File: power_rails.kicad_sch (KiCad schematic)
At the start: 26 parts, among them SW3 ~{SR}, SW4 ~{PB}, U12 MCP1799x-500xxTT, U5 AP63200WU, U7 AP63205WU, U8 STM6601, U9 TPS62162DSG

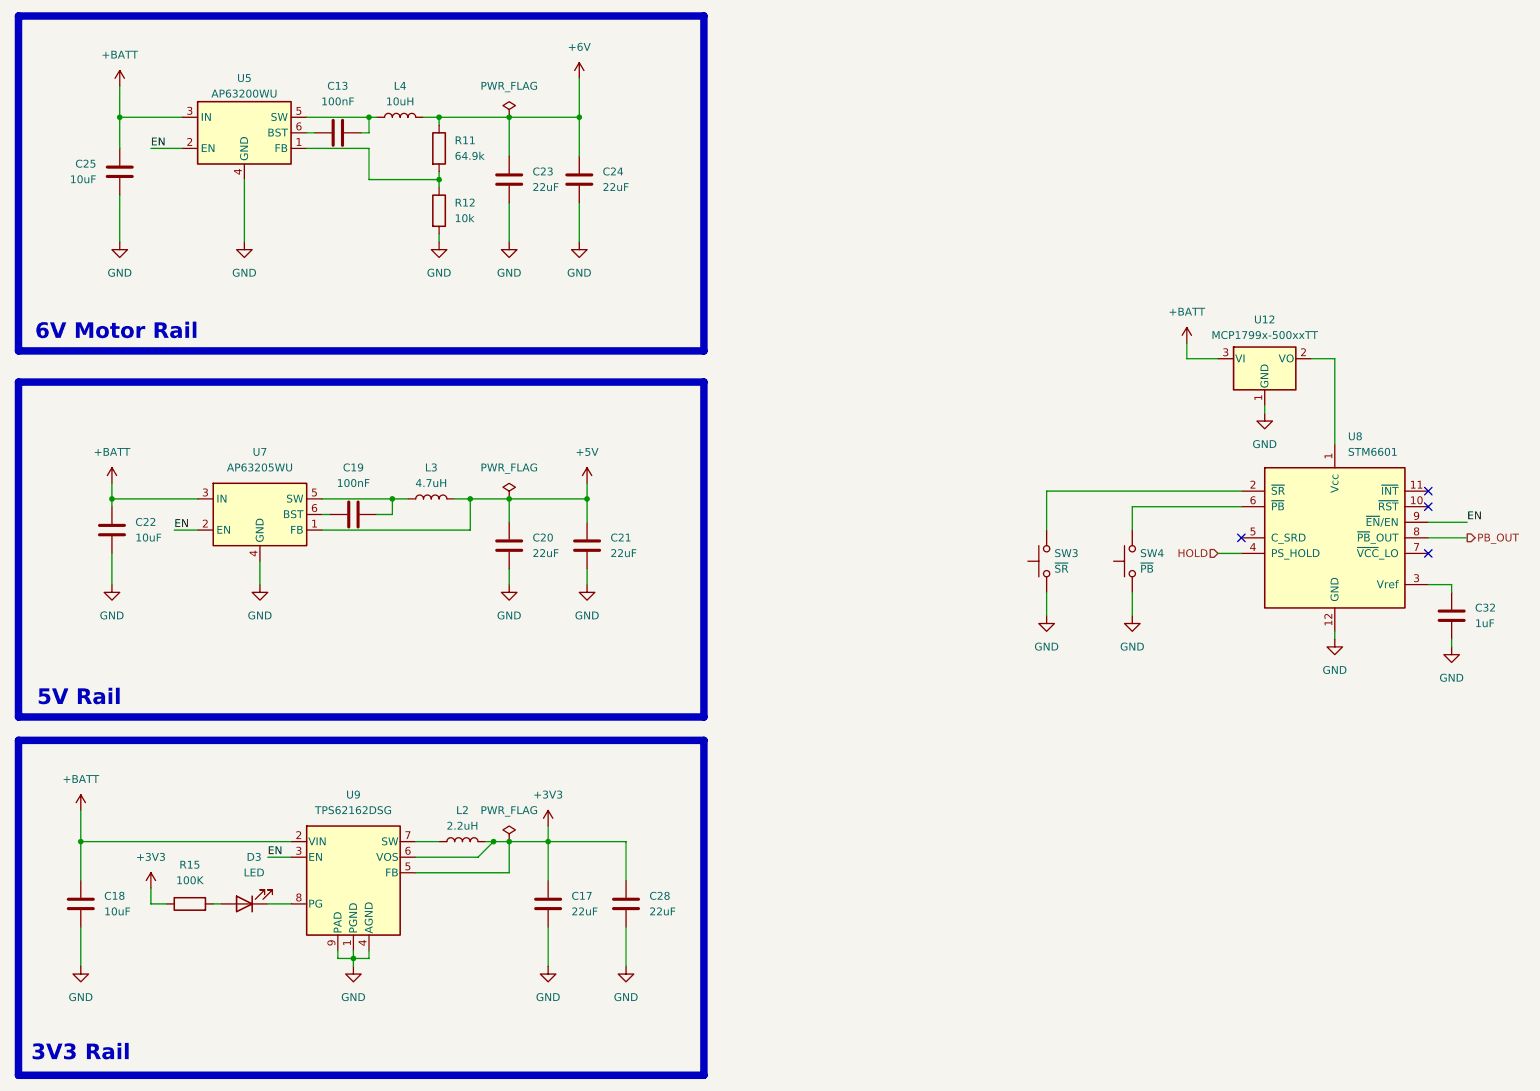
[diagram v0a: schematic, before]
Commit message: annotate with LCSC components
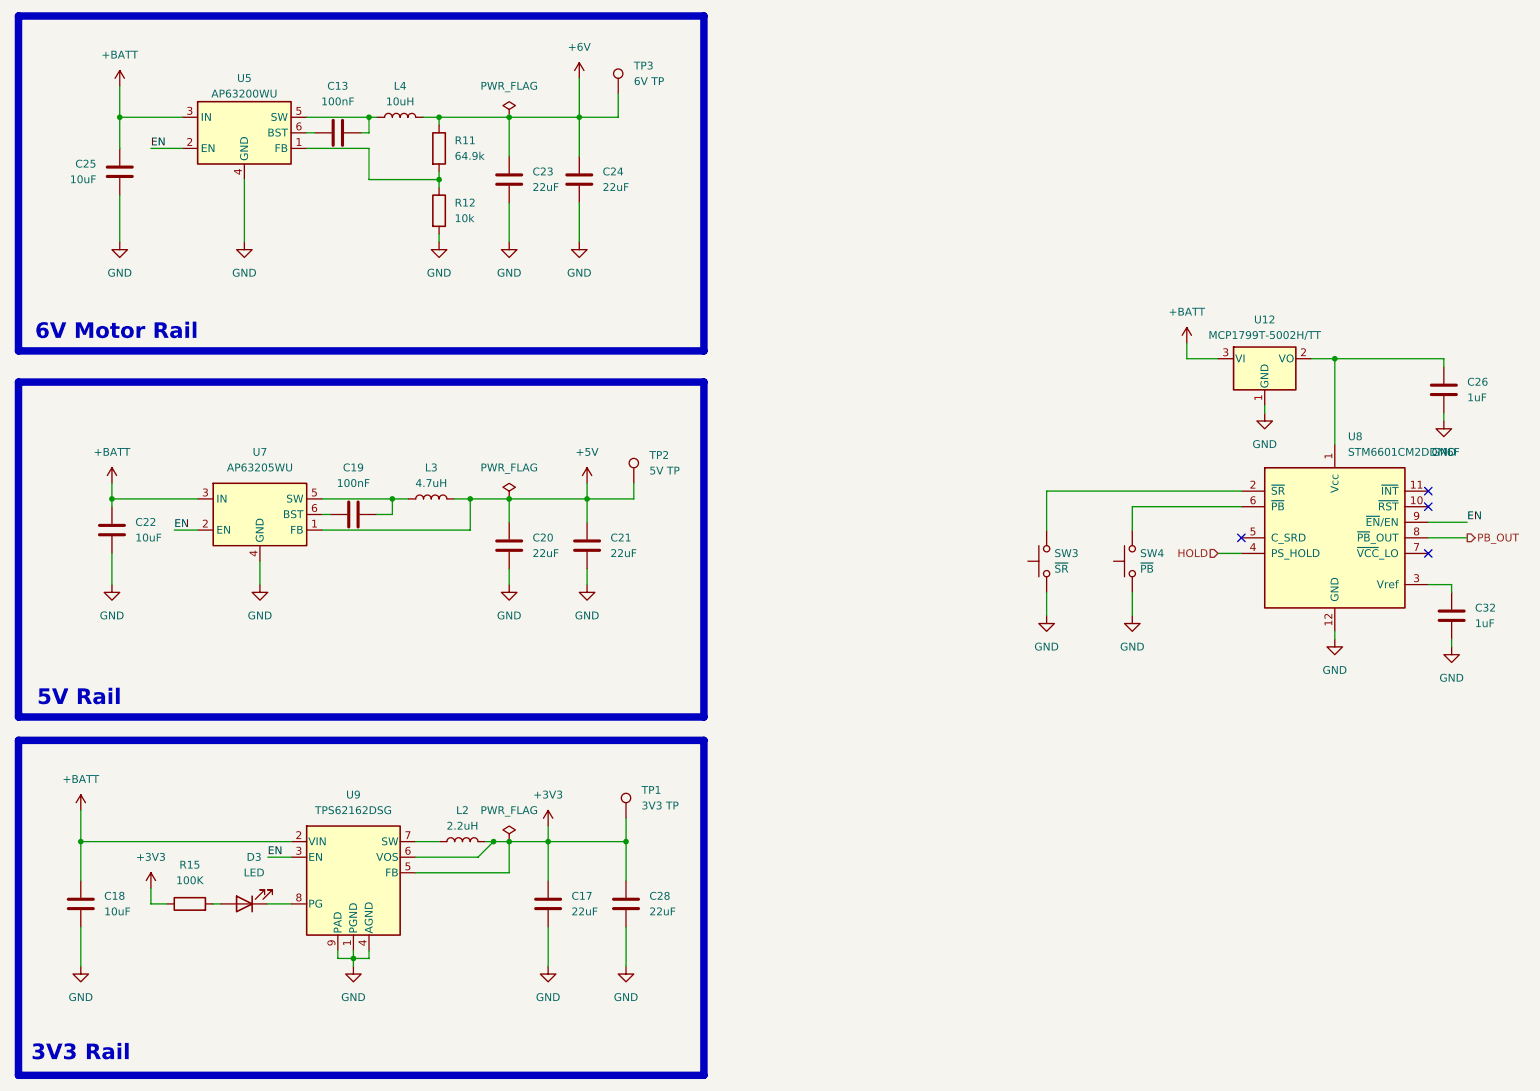
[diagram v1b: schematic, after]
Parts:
- added C26: 1uF, Capacitor_SMD:C_0603_1608Metric, symbol Device:C
- added TP1: 3V3 TP, TestPoint:TestPoint_Pad_D1.0mm, symbol Connector:TestPoint
- added TP2: 5V TP, TestPoint:TestPoint_Pad_D1.0mm, symbol Connector:TestPoint
- added TP3: 6V TP, TestPoint:TestPoint_Pad_D1.0mm, symbol Connector:TestPoint
- C32: LCSC (none) -> C5673; MPN (none) -> CL10A105KA8NNNC; Manufacturer (none) -> Samsung Electro-Mechanics
- U12: value MCP1799x-500xxTT -> MCP1799T-5002H/TT; LCSC (none) -> C2890492; MPN (none) -> MCP1799T-5002H/TT; Manufacturer (none) -> Microchip Technology
- U8: value STM6601 -> STM6601CM2DDM6F; LCSC (none) -> C155599; MPN (none) -> STM6601CM2DDM6F; Manufacturer (none) -> STMicroelectronics
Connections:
- net +3V3: now also TP1.1
- net +5V: now also TP2.1
- net +6V: now also TP3.1
- net GND: now also C26.2
- net at U12.2 (VO), U8.1 (Vcc): now also C26.1

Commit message: finalized component selection
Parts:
- added C31: 1uF, Capacitor_SMD:C_0603_1608Metric, symbol Device:C
- C26: value 1uF -> 2.2uF; LCSC C5673 -> C415535; MPN CL10A105KA8NNNC -> (none); Manufacturer Samsung Electro-Mechanics -> (none)
- L2: footprint Inductor_SMD:L_APV_ANR3012 -> Inductor_SMD:L_Coilcraft_LPS3010
- L3: footprint Inductor_SMD:L_Sunlord_MWSA0503S -> Inductor_SMD:L_Chilisin_BWVS00505030
- L4: LCSC C431344 -> C408412; MPN CMLW5040S100MST -> (none); Manufacturer Cybermax -> Sunlord
- R12: LCSC C2906982 -> C15401; MPN FRC0603F1002TS -> (none); Manufacturer FOJAN -> UNI-ROYAL(Uniroyal Elec)
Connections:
- net +BATT: now also C31.1
- net GND: now also C31.2
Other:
- moved on the sheet: C26, U12

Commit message: add MPS entries
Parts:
- C13, C19: MPN CC0603KRX7R9BB104 -> GPN; Manufacturer YAGEO -> Generic
- C17, C20, C21, C23, C24, C28: MPN CL21A226KOQNNNE -> GPN; Manufacturer Samsung Electro-Mechanics -> Generic
- C18, C22, C25: MPN GRM21BR61E106KA73L -> GPN; Manufacturer muRata -> Generic
- C26, C31: MPN (none) -> GPN; Manufacturer (none) -> Generic
- C32: MPN CL10A105KA8NNNC -> GPN; Manufacturer Samsung Electro-Mechanics -> Generic
- D3: MPN KT-0603R -> 150060RS75000; Manufacturer Hubei KENTO Elec -> Wurth Elektronik
- R11: MPN 0603WAF6492T5E -> GPN; Manufacturer UNI-ROYAL -> Generic
- R12: MPN (none) -> GPN; Manufacturer UNI-ROYAL(Uniroyal Elec) -> Generic
- R15: MPN 0603WAF1003T5E -> GPN; Manufacturer UNI-ROYAL -> Generic
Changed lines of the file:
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@@
 			)
 		)
-		(property "Manufacturer" "Samsung Electro-Mechanics"
+		(property "Manufacturer" "Generic"
 			(at 0 0 0)
 			(hide yes)
@@
 			)
 		)
-		(property "MPN" "CL21A226KOQNNNE"
+		(property "MPN" "GPN"
 			(at 0 0 0)
 			(hide yes)
@@
 			)
 		)
+		(property "Manufacturer" "Generic" (at 0 0 0)
+			(effects
+				(font
+					(size 1.27 1.27)
+				)
+				(hide yes)
+			)
+		)
+		(property "MPN" "GPN" (at 0 0 0)
+			(effects
+				(font
+					(size 1.27 1.27)
+				)
+				(hide yes)
+			)
+		)
 		(pin "1"
 		)
@@
 			)
 		)
-		(property "Manufacturer" "Samsung Electro-Mechanics"
+		(property "Manufacturer" "Generic"
 			(at 0 0 0)
 			(hide yes)
@@
 			)
 		)
-		(property "MPN" "CL21A226KOQNNNE"
+		(property "MPN" "GPN"
 			(at 0 0 0)
 			(hide yes)
@@
 			)
 		)
-		(property "Manufacturer" "UNI-ROYAL"
+		(property "Manufacturer" "Generic"
 			(at 0 0 0)
 			(hide yes)
@@
 			)
 		)
-		(property "MPN" "0603WAF6492T5E"
+		(property "MPN" "GPN"
 			(at 0 0 0)
 			(hide yes)
@@
 			)
 		)
-		(property "Manufacturer" "Samsung Electro-Mechanics"
+		(property "Manufacturer" "Generic"
 			(at 0 0 0)
 			(hide yes)
@@
 			)
 		)
-		(property "MPN" "CL21A226KOQNNNE"
+		(property "MPN" "GPN"
 			(at 0 0 0)
 			(hide yes)
@@
 			)
 		)
-		(property "Manufacturer" "YAGEO"
+		(property "Manufacturer" "Generic"
 			(at 0 0 0)
 			(hide yes)
@@
 			)
 		)
-		(property "MPN" "CC0603KRX7R9BB104"
+		(property "MPN" "GPN"
 			(at 0 0 0)
 			(hide yes)
@@
 			)
 		)
-		(property "Manufacturer" "YAGEO"
+		(property "Manufacturer" "Generic"
 			(at 0 0 0)
 			(hide yes)
@@
 			)
 		)
-		(property "MPN" "CC0603KRX7R9BB104"
+		(property "MPN" "GPN"
 			(at 0 0 0)
 			(hide yes)
@@
 			)
 		)
-		(property "Manufacturer" "Samsung Electro-Mechanics"
+		(property "Manufacturer" "Generic"
 			(at 0 0 0)
 			(hide yes)
@@
 			)
 		)
-		(property "MPN" "CL21A226KOQNNNE"
+		(property "MPN" "GPN"
 			(at 0 0 0)
 			(hide yes)
@@
 			)
 		)
-		(property "Manufacturer" "muRata"
+		(property "Manufacturer" "Generic"
 			(at 0 0 0)
 			(hide yes)
@@
 			)
 		)
-		(property "MPN" "GRM21BR61E106KA73L"
+		(property "MPN" "GPN"
 			(at 0 0 0)
 			(hide yes)
@@
 			)
 		)
-		(property "Manufacturer" "Samsung Electro-Mechanics"
+		(property "Manufacturer" "Generic"
 			(at 0 0 0)
 			(hide yes)
@@
 			)
 		)
-		(property "MPN" "CL21A226KOQNNNE"
+		(property "MPN" "GPN"
 			(at 0 0 0)
 			(hide yes)
@@
 			)
 		)
-		(property "Manufacturer" "muRata"
+		(property "Manufacturer" "Generic"
 			(at 0 0 0)
 			(hide yes)
@@
 			)
 		)
-		(property "MPN" "GRM21BR61E106KA73L"
+		(property "MPN" "GPN"
 			(at 0 0 0)
 			(hide yes)
@@
 			)
 		)
-		(property "Manufacturer" "UNI-ROYAL(Uniroyal Elec)"
+		(property "Manufacturer" "Generic"
 			(at 0 0 0)
 			(hide yes)
@@
 			)
 		)
-		(property "MPN" ""
+		(property "MPN" "GPN"
 			(at 0 0 0)
 			(hide yes)
@@
 			)
 		)
-		(property "MPN" ""
+		(property "MPN" "GPN"
 			(at -7.62 -3.81 0)
 			(hide yes)
@@
 			)
 		)
-		(property "Manufacturer" ""
+		(property "Manufacturer" "Generic"
 			(at -7.62 -3.81 0)
 			(hide yes)
@@
 			)
 		)
-		(property "Manufacturer" "Samsung Electro-Mechanics"
+		(property "Manufacturer" "Generic"
 			(at 0 0 0)
 			(hide yes)
@@
 			)
 		)
-		(property "MPN" "CL21A226KOQNNNE"
+		(property "MPN" "GPN"
 			(at 0 0 0)
 			(hide yes)
@@
 			)
 		)
-		(property "Manufacturer" "UNI-ROYAL"
+		(property "Manufacturer" "Generic"
 			(at 0 0 0)
 			(hide yes)
@@
 			)
 		)
-		(property "MPN" "0603WAF1003T5E"
+		(property "MPN" "GPN"
 			(at 0 0 0)
 			(hide yes)
@@
 			)
 		)
-		(property "Manufacturer" "Hubei KENTO Elec"
+		(property "Manufacturer" "Wurth Elektronik"
 			(at 0 0 0)
 			(hide yes)
@@
 			)
 		)
-		(property "MPN" "KT-0603R"
+		(property "MPN" "150060RS75000"
 			(at 0 0 0)
 			(hide yes)
@@
 			)
 		)
-		(property "Manufacturer" "muRata"
+		(property "Manufacturer" "Generic"
 			(at 0 0 0)
 			(hide yes)
@@
 			)
 		)
-		(property "MPN" "GRM21BR61E106KA73L"
+		(property "MPN" "GPN"
 			(at 0 0 0)
 			(hide yes)
@@
 			)
 		)
-		(property "MPN" "CL10A105KA8NNNC"
+		(property "MPN" "GPN"
 			(at 0 0 0)
 			(hide yes)
@@
 			)
 		)
-		(property "Manufacturer" "Samsung Electro-Mechanics"
+		(property "Manufacturer" "Generic"
 			(at 0 0 0)
 			(hide yes)

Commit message: update MPN codes
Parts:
- C13, C19: MPN GPN -> GPC0603104
- C17, C20, C21, C23, C24, C28: MPN GPN -> GPC0805226
- C18, C22, C25: MPN GPN -> GPC0805106
- C26: MPN GPN -> GPC0603225
- C31, C32: MPN GPN -> GPC0603105
- R11: MPN GPN -> GPR0603649
- R12: MPN GPN -> GPR060310K
- R15: MPN GPN -> GPR0603100K
- TP1, TP2, TP3: now left out of the parts list
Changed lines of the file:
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@@
 			)
 		)
-		(property "MPN" "GPN"
+		(property "MPN" "GPC0805226"
 			(at 0 0 0)
 			(hide yes)
@@
 			)
 		)
-		(property "Manufacturer" "Generic" (at 0 0 0)
+		(property "Manufacturer" "Generic"
+			(at 0 0 0)
+			(hide yes)
+			(show_name no)
+			(do_not_autoplace no)
 			(effects
 				(font
 					(size 1.27 1.27)
 				)
-				(hide yes)
 			)
 		)
-		(property "MPN" "GPN" (at 0 0 0)
+		(property "MPN" "GPC0603105"
+			(at 0 0 0)
+			(hide yes)
+			(show_name no)
+			(do_not_autoplace no)
 			(effects
 				(font
 					(size 1.27 1.27)
 				)
-				(hide yes)
 			)
 		)
@@
 		(body_style 1)
 		(exclude_from_sim no)
-		(in_bom yes)
+		(in_bom no)
 		(on_board yes)
 		(in_pos_files yes)
@@
 			)
 		)
-		(property "MPN" "GPN"
+		(property "MPN" "GPC0805226"
 			(at 0 0 0)
 			(hide yes)
@@
 			)
 		)
-		(property "MPN" "GPN"
+		(property "MPN" "GPR0603649"
 			(at 0 0 0)
 			(hide yes)
@@
 			)
 		)
-		(property "MPN" "GPN"
+		(property "MPN" "GPC0805226"
 			(at 0 0 0)
 			(hide yes)
@@
 			)
 		)
-		(property "MPN" "GPN"
+		(property "MPN" "GPC0603104"
 			(at 0 0 0)
 			(hide yes)
@@
 			)
 		)
-		(property "MPN" "GPN"
+		(property "MPN" "GPC0603104"
 			(at 0 0 0)
 			(hide yes)
@@
 		(body_style 1)
 		(exclude_from_sim no)
-		(in_bom yes)
+		(in_bom no)
 		(on_board yes)
 		(in_pos_files yes)
@@
 			)
 		)
-		(property "MPN" "GPN"
+		(property "MPN" "GPC0805226"
 			(at 0 0 0)
 			(hide yes)
@@
 			)
 		)
-		(property "MPN" "GPN"
+		(property "MPN" "GPC0805106"
 			(at 0 0 0)
 			(hide yes)
@@
 			)
 		)
-		(property "MPN" "GPN"
+		(property "MPN" "GPC0805226"
 			(at 0 0 0)
 			(hide yes)
@@
 			)
 		)
-		(property "MPN" "GPN"
+		(property "MPN" "GPC0805106"
 			(at 0 0 0)
 			(hide yes)
@@
 			)
 		)
-		(property "MPN" "GPN"
+		(property "MPN" "GPR060310K"
 			(at 0 0 0)
 			(hide yes)
@@
 		(body_style 1)
 		(exclude_from_sim no)
-		(in_bom yes)
+		(in_bom no)
 		(on_board yes)
 		(in_pos_files yes)
@@
 			)
 		)
-		(property "MPN" "GPN"
+		(property "MPN" "GPC0603225"
 			(at -7.62 -3.81 0)
 			(hide yes)
@@
 			)
 		)
-		(property "MPN" "GPN"
+		(property "MPN" "GPC0805226"
 			(at 0 0 0)
 			(hide yes)
@@
 			)
 		)
-		(property "MPN" "GPN"
+		(property "MPN" "GPR0603100K"
 			(at 0 0 0)
 			(hide yes)
@@
 			)
 		)
-		(property "MPN" "GPN"
+		(property "MPN" "GPC0805106"
 			(at 0 0 0)
 			(hide yes)
@@
 			)
 		)
-		(property "MPN" "GPN"
+		(property "MPN" "GPC0603105"
 			(at 0 0 0)
 			(hide yes)
